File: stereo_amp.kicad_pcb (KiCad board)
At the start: 2 copper layers, 125 x 28 mm, 116 parts, among them J101 HEADER1X2, J102 HEADER1X2, J103 HEADER1X2, J104 HEADER1X2, J105 HEADER1X5, J106 VCCL, J107 VCCR, J108 HEADER1X5, J109 HEADER1X2, J110 HEADER1X2, Q201 BC309B, Q202 BC237B, Q203 BD135, Q204 BD136, Q205 BD243C, Q206 BD244C, Q301 BC309B, Q302 BC237B, Q303 BD135, Q304 BD136, Q305 BD243C, Q306 BD244C

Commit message: Finished placement and routing.
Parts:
- added J111: HEADER1X3, Pinhead:HEADER1x3V, F.Cu at (43.0, 129.5)
- added J112: HEADER1X3, Pinhead:HEADER1x3V, F.Cu at (131.0, 129.5)
- added MountHole_D35P80: VAL**, Newlib:MountHole_D35P80, F.Cu at (56.0, 126.5)
- added MountHole_D35P80: VAL**, Newlib:MountHole_D35P80, F.Cu at (123.0, 126.5)
- added MountHole_D35P80: VAL**, Newlib:MountHole_D35P80, F.Cu at (140.0, 81.5)
- added MountHole_D35P80: VAL**, Newlib:MountHole_D35P80, F.Cu at (39.0, 81.5)
- C306, R301, R302, R303, R304, R305, R306, R307, R308, R309, R310, R311, R312, R313, R316, R317, R318, R321: moved to B.Cu
- J105, J108: value HEADER1X5 -> HEADER1X3; footprint Pinhead:HEADER1x5V -> Pinhead:HEADER1x3V
- R219, R319: footprint Newlib:RESA_D40L110 -> Newlib:RESR_D40P40
- moved J108 217.4 mm to (53.0, 139.0), turned to 180 degrees
- moved R321 184.0 mm to (101.2, 78.5)
- moved R318 166.8 mm to (114.0, 83.5), turned to 180 degrees
- moved C309 166.2 mm to (109.5, 96.5)
- moved C304 165.5 mm to (127.2, 107.8), turned to 180 degrees
- moved R313 164.0 mm to (121.2, 78.0), turned to 270 degrees
- moved Q306 163.7 mm to (103.0, 74.5), turned to 180 degrees
- moved R316 161.1 mm to (120.2, 88.5), turned to 90 degrees
- moved R301 159.7 mm to (134.5, 119.5), turned to 270 degrees
- moved R317 155.1 mm to (115.2, 88.5), turned to 270 degrees
- moved C301 155.0 mm to (132.2, 119.5), turned to 270 degrees
- moved R304 152.9 mm to (129.0, 119.5), turned to 270 degrees
- moved R302 151.9 mm to (131.0, 119.5), turned to 270 degrees
- moved R312 151.0 mm to (123.2, 95.2), turned to 270 degrees
- moved Q304 150.1 mm to (113.0, 73.5), turned to 180 degrees
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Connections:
- J105 pad 2: /Filters/OUT_R -> /Filters/OUT_L
- J108 pad 2: /Right Channel/IN -> /Filters/OUT_R
- R215 pad 1: Net-(C207-Pad2) -> Net-(R215-Pad1)
- R215 pad 3: Net-(R215-Pad3) -> Net-(C207-Pad2)
- R217 pad 2: Net-(R215-Pad3) -> Net-(R215-Pad1)
- R218 pad 2: Net-(R215-Pad3) -> Net-(R215-Pad1)
- R219 pad 1: Net-(R215-Pad3) -> Net-(R215-Pad1)
- R315 pad 1: Net-(C307-Pad2) -> Net-(R315-Pad1)
- R315 pad 3: Net-(R315-Pad3) -> Net-(C307-Pad2)
- R317 pad 2: Net-(R315-Pad3) -> Net-(R315-Pad1)
- R318 pad 2: Net-(R315-Pad3) -> Net-(R315-Pad1)
- R319 pad 1: Net-(R315-Pad3) -> Net-(R315-Pad1)
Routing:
- net GND: track 55.0 -> 301.2 mm, vias 4 -> 3
- net /Power Supply Left/OUT: track 0.00 -> 107.4 mm
- net /Power Supply Right/OUT: track 0.00 -> 101.8 mm
- net Net-(C307-Pad2): track 0.00 -> 53.5 mm
- net Net-(C309-Pad1): track 0.00 -> 53.0 mm
- net Net-(C209-Pad1): track 0.00 -> 47.6 mm
- net /Power Supply Right/IN2: track 0.00 -> 45.2 mm
- net Net-(C305-Pad1): track 0.00 -> 42.8 mm
- net Net-(C207-Pad2): track 0.00 -> 41.8 mm
- net Net-(C205-Pad1): track 0.00 -> 40.4 mm
- net /Power Supply Left/IN1: track 0.00 -> 34.9 mm
- net Net-(Q302-Pad1): track 0.00 -> 31.2 mm
- net Net-(Q202-Pad1): track 0.00 -> 31.0 mm
- net Net-(C308-Pad2): track 0.00 -> 30.3 mm
- net /Power Supply Left/IN2: track 0.00 -> 26.4 mm
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- added copper zone on F.Cu, net GND
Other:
- board size 125 x 28 mm -> 125 x 94 mm

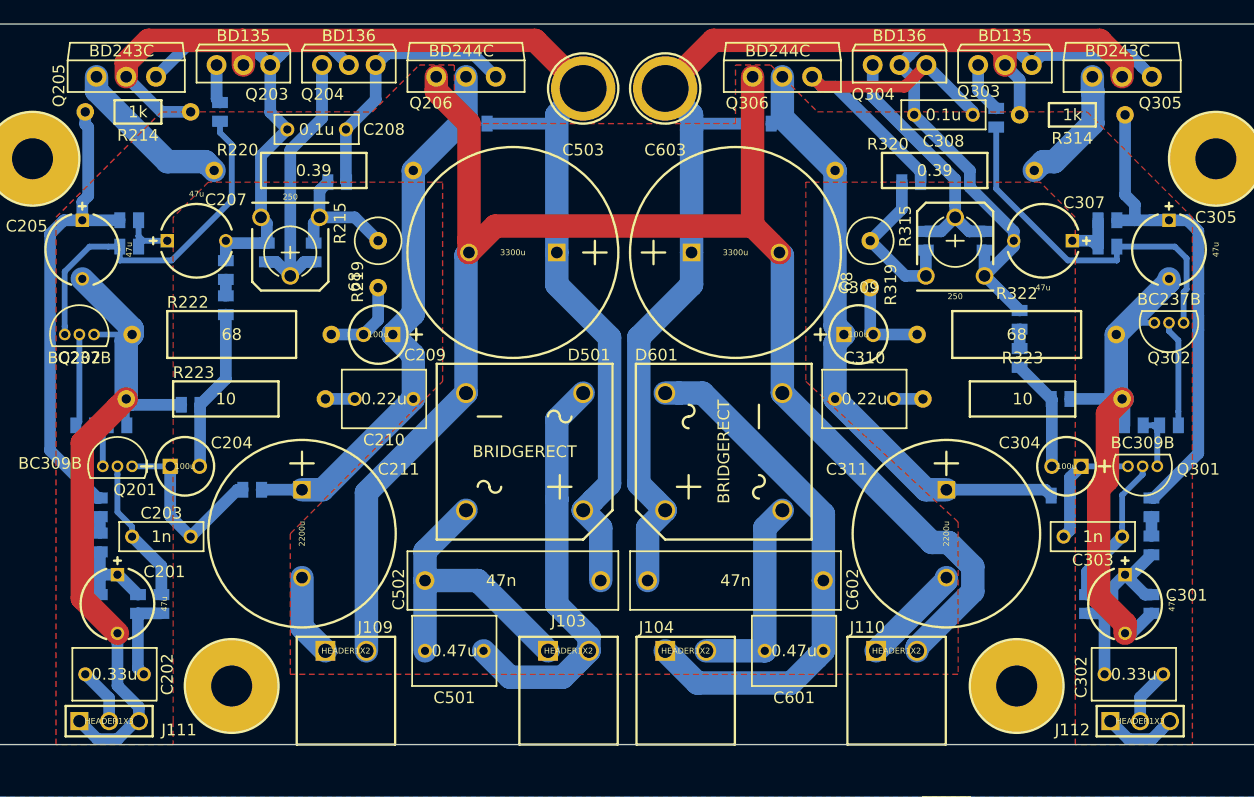
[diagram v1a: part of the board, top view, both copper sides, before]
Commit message: Fixed transistors with swapped E-C
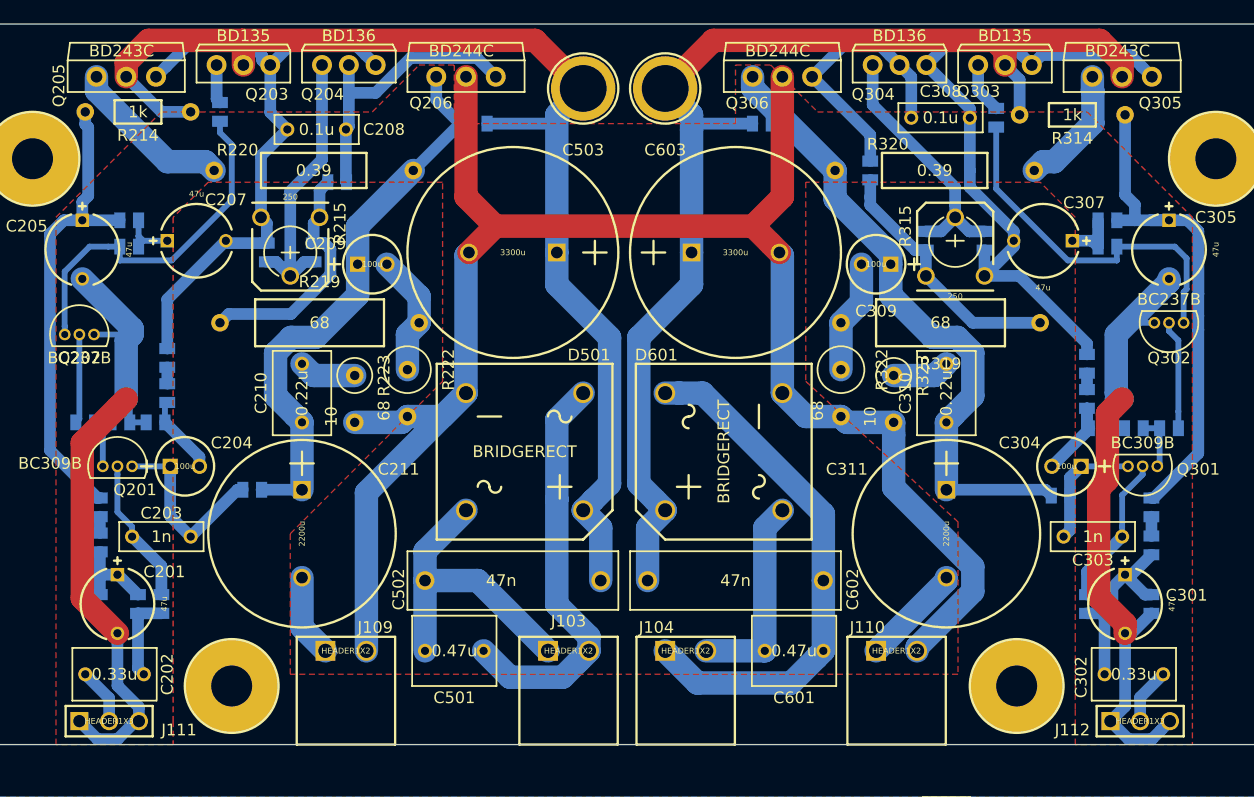
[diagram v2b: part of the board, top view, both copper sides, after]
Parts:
- R219, R319: footprint Newlib:RESR_D40P40 -> Newlib:RESA_D40L110
- R222, R322: footprint Newlib:RESA_D40L110 -> Newlib:RESR_D40P40
- R223, R323: footprint Newlib:RESA_D30L90 -> Newlib:RESR_D30P40
- moved R222 15.3 mm to (71.0, 99.5), turned to 270 degrees
- moved R322 15.3 mm to (108.0, 99.5), turned to 270 degrees
- moved R223 11.2 mm to (66.5, 100.0), turned to 270 degrees
- moved R323 11.2 mm to (112.5, 100.0), turned to 270 degrees
- moved R319 9.22 mm to (116.5, 95.5), turned to 180 degrees
- moved C206 9.01 mm to (50.5, 101.5)
- moved R212 9.01 mm to (50.5, 98.5)
- moved R219 8.60 mm to (63.5, 95.5), turned to 0 degrees
- moved C210 7.02 mm to (62.0, 101.5), turned to 90 degrees
- moved C310 7.02 mm to (117.0, 101.5), turned to 90 degrees
- moved R312 6.86 mm to (129.0, 99.0)
- moved C306 6.73 mm to (129.0, 102.0)
- moved C309 6.18 mm to (111.0, 90.5), turned to 180 degrees
- moved C209 6.02 mm to (68.0, 90.5), turned to 0 degrees
- moved R307 4.10 mm to (130.0, 104.5)
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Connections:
- Q204 pad 1: Net-(C208-Pad2) -> Net-(C207-Pad2)
- Q204 pad 2: Net-(C207-Pad2) -> Net-(C208-Pad2)
- Q206 pad 2: Net-(C209-Pad1) -> GND
- Q206 pad 3: GND -> Net-(C209-Pad1)
- Q304 pad 1: Net-(C308-Pad2) -> Net-(C307-Pad2)
- Q304 pad 2: Net-(C307-Pad2) -> Net-(C308-Pad2)
- Q306 pad 2: Net-(C309-Pad1) -> GND
- Q306 pad 3: GND -> Net-(C309-Pad1)
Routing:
- net GND: track 301.2 -> 313.5 mm
- net Net-(C207-Pad2): track 41.8 -> 53.8 mm
- net Net-(R215-Pad1): track 11.5 -> 20.6 mm
- net Net-(R315-Pad1): track 14.3 -> 22.1 mm
- net Net-(C204-Pad2): track 13.9 -> 6.83 mm
- net Net-(C308-Pad2): track 30.3 -> 23.4 mm
- net Net-(C307-Pad2): track 53.5 -> 58.1 mm
- net Net-(C209-Pad2): track 7.27 -> 10.6 mm
- net Net-(C309-Pad1): track 53.0 -> 55.4 mm
- net Net-(C310-Pad2): track 2.50 -> 4.91 mm
- net Net-(C210-Pad2): track 2.50 -> 4.91 mm
- net Net-(C208-Pad2): track 22.6 -> 24.6 mm
- net Net-(C309-Pad2): track 7.85 -> 9.73 mm
- net Net-(C304-Pad2): track 9.59 -> 7.98 mm
- net Net-(C209-Pad1): track 47.6 -> 48.9 mm
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
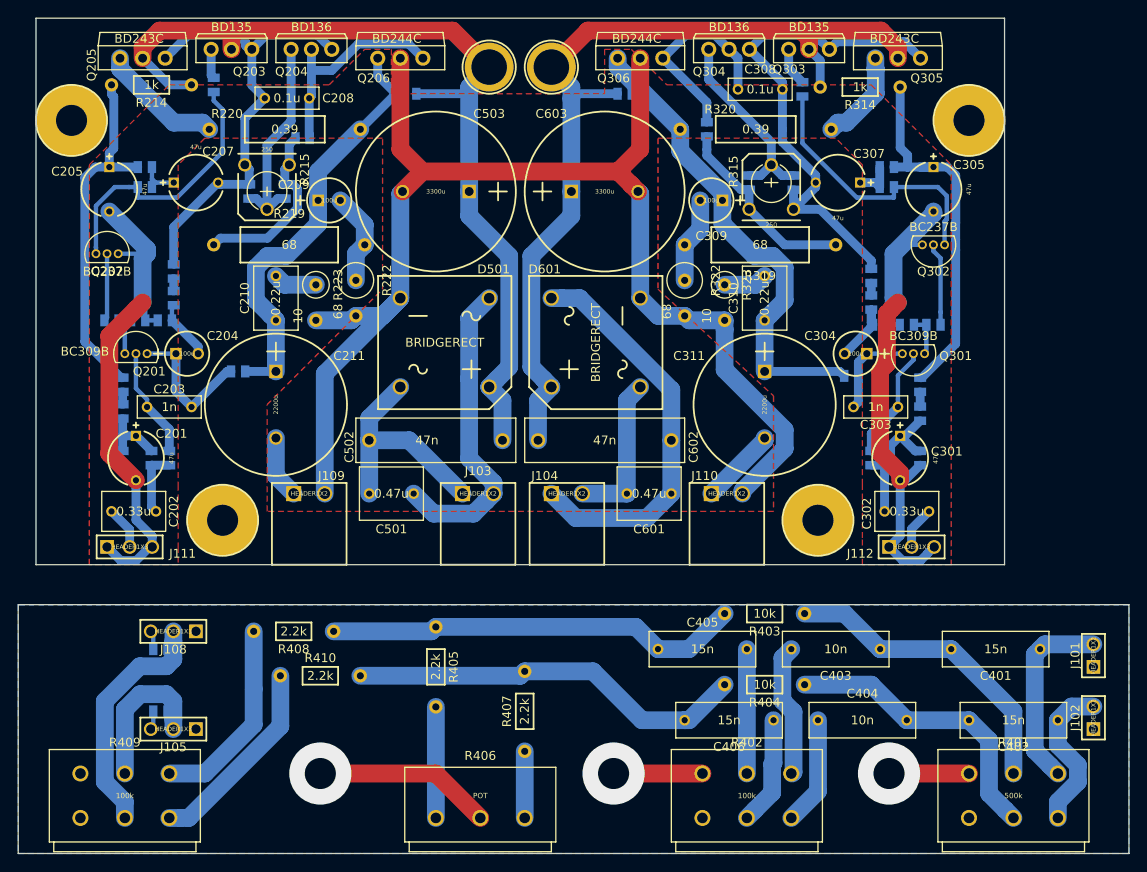
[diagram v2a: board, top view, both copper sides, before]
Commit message: Updated PCB layout to reflect changes in footprints.
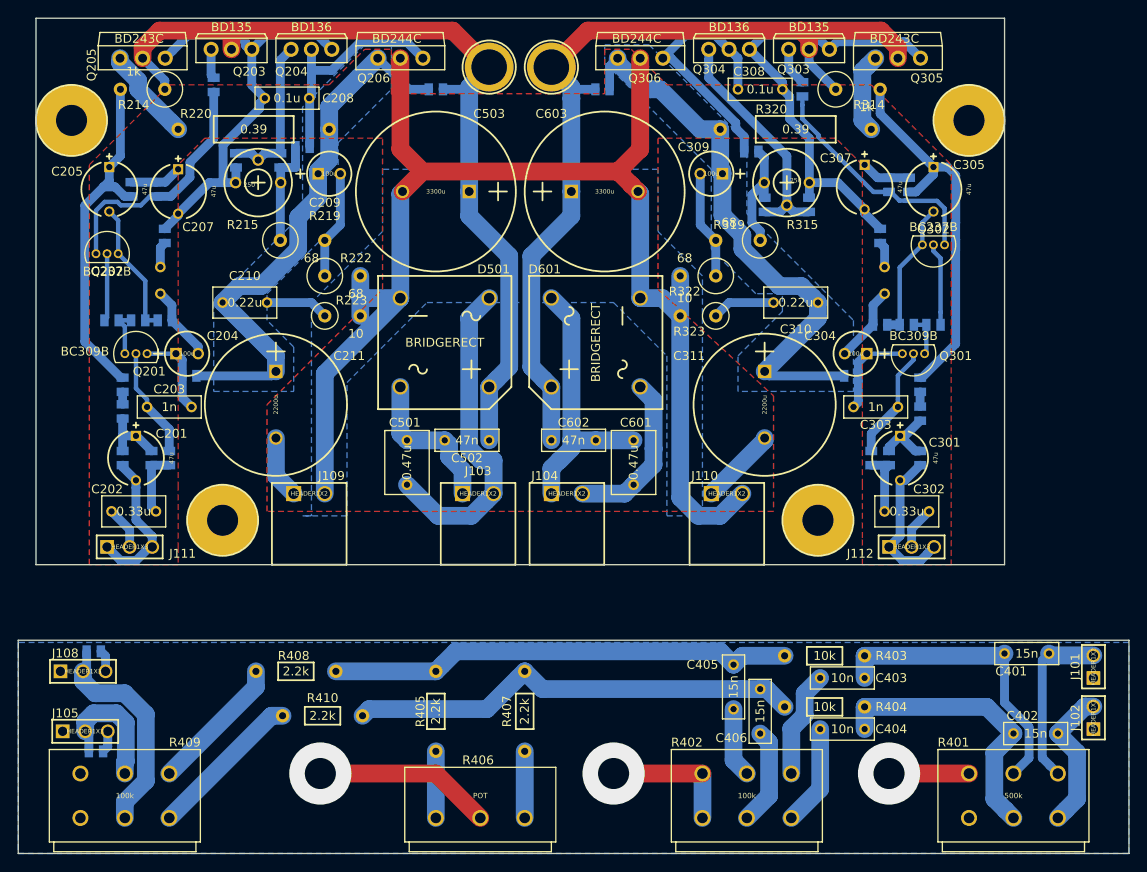
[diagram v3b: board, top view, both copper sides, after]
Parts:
- C202, C302: footprint Newlib:CAPRR_P50W45L72 -> Newlib:CAPRR_P50W35L72
- C206, C306: footprint Newlib:C0805 -> Newlib:CAPRR_P30W20L40
- C210, C310: footprint Newlib:CAPRR_P50W50L72 -> Newlib:CAPRR_P50W35L72
- C401, C402, C403, C404, C405, C406: footprint Newlib:CAPRR_P100W40L125 -> Newlib:CAPRR_P50W25L72
- C501, C601: footprint Newlib:CAPRR_P50W60L72 -> Newlib:CAPRR_P50W50L72
- C502, C602: footprint Newlib:CAPRR_P150W50L180 -> Newlib:CAPRR_P50W25L72
- R201, R202, R203, R204, R205, R206, R207, R208, R209, R210, R211, R212, R213, R216, R217, R218, R221, R301, R302, R303, R304, R305, R306, R307, R308, R309, R310, R311, R312, R313, R316, R317, R318, R321: footprint Newlib:C0805 -> Newlib:R0805
- R214, R314: footprint Newlib:RESA_D20L40 -> Newlib:RESR_D40P50
- R215, R315: footprint Newlib:RM-65 -> Newlib:POT-3339P
- R219, R319: footprint Newlib:RESA_D40L110 -> Newlib:RESR_D40P50
- moved J108 15.9 mm to (37.8, 143.5), turned to 0 degrees
- moved J105 15.0 mm to (38.0, 150.2), turned to 0 degrees
- moved C407 8.53 mm to (41.8, 152.5), turned to 0 degrees
- moved R403 8.25 mm to (123.8, 141.8)
- moved C408 7.50 mm to (41.5, 141.2), turned to 0 degrees
- moved R404 7.20 mm to (123.8, 147.5)
- moved R318 5.59 mm to (115.5, 85.0), turned to 0 degrees
- moved R211 5.52 mm to (52.2, 110.2)
- moved C405 5.51 mm to (113.5, 145.2), turned to 270 degrees
- moved R405 5.00 mm to (80.0, 148.0)
- moved R312 4.61 mm to (130.0, 94.5)
- moved R408 4.51 mm to (64.2, 143.5)
- moved R410 4.51 mm to (67.2, 148.5)
- moved R320 4.50 mm to (120.5, 82.5)
- moved R212 4.12 mm to (49.5, 94.5)
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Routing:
- net GND: track 313.5 -> 268.2 mm
- net /Power Supply Right/IN2: track 45.2 -> 30.9 mm
- net Net-(C209-Pad1): track 48.9 -> 63.0 mm
- net Net-(R315-Pad1): track 22.1 -> 12.9 mm
- net /Power Supply Left/IN2: track 26.4 -> 17.4 mm
- net Net-(C309-Pad1): track 55.4 -> 64.2 mm
- net Net-(R215-Pad1): track 20.6 -> 12.2 mm
- net Net-(R408-Pad2): track 22.3 -> 15.5 mm
- net Net-(C307-Pad2): track 58.1 -> 51.6 mm
- net Net-(Q204-Pad3): track 24.1 -> 17.8 mm
- net Net-(C405-Pad2): track 14.0 -> 7.87 mm
- net Net-(C203-Pad2): track 16.7 -> 10.6 mm
- net Net-(C406-Pad2): track 45.1 -> 51.2 mm
- net /Power Supply Left/OUT: track 107.4 -> 101.3 mm
- net Net-(C308-Pad2): track 23.4 -> 29.0 mm
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- added copper zone on B.Cu, net Net-(C209-Pad1)
- added copper zone on B.Cu, net Net-(C309-Pad1)
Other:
- outline, holes or cut-outs redrawn
